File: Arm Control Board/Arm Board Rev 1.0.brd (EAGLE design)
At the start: 189.8 x 119.2 mm, 54 parts

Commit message: test
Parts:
- moved B1 85.2 mm to (78.0, 74.0)
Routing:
- net TX: track 133.4 -> 132.8 mm

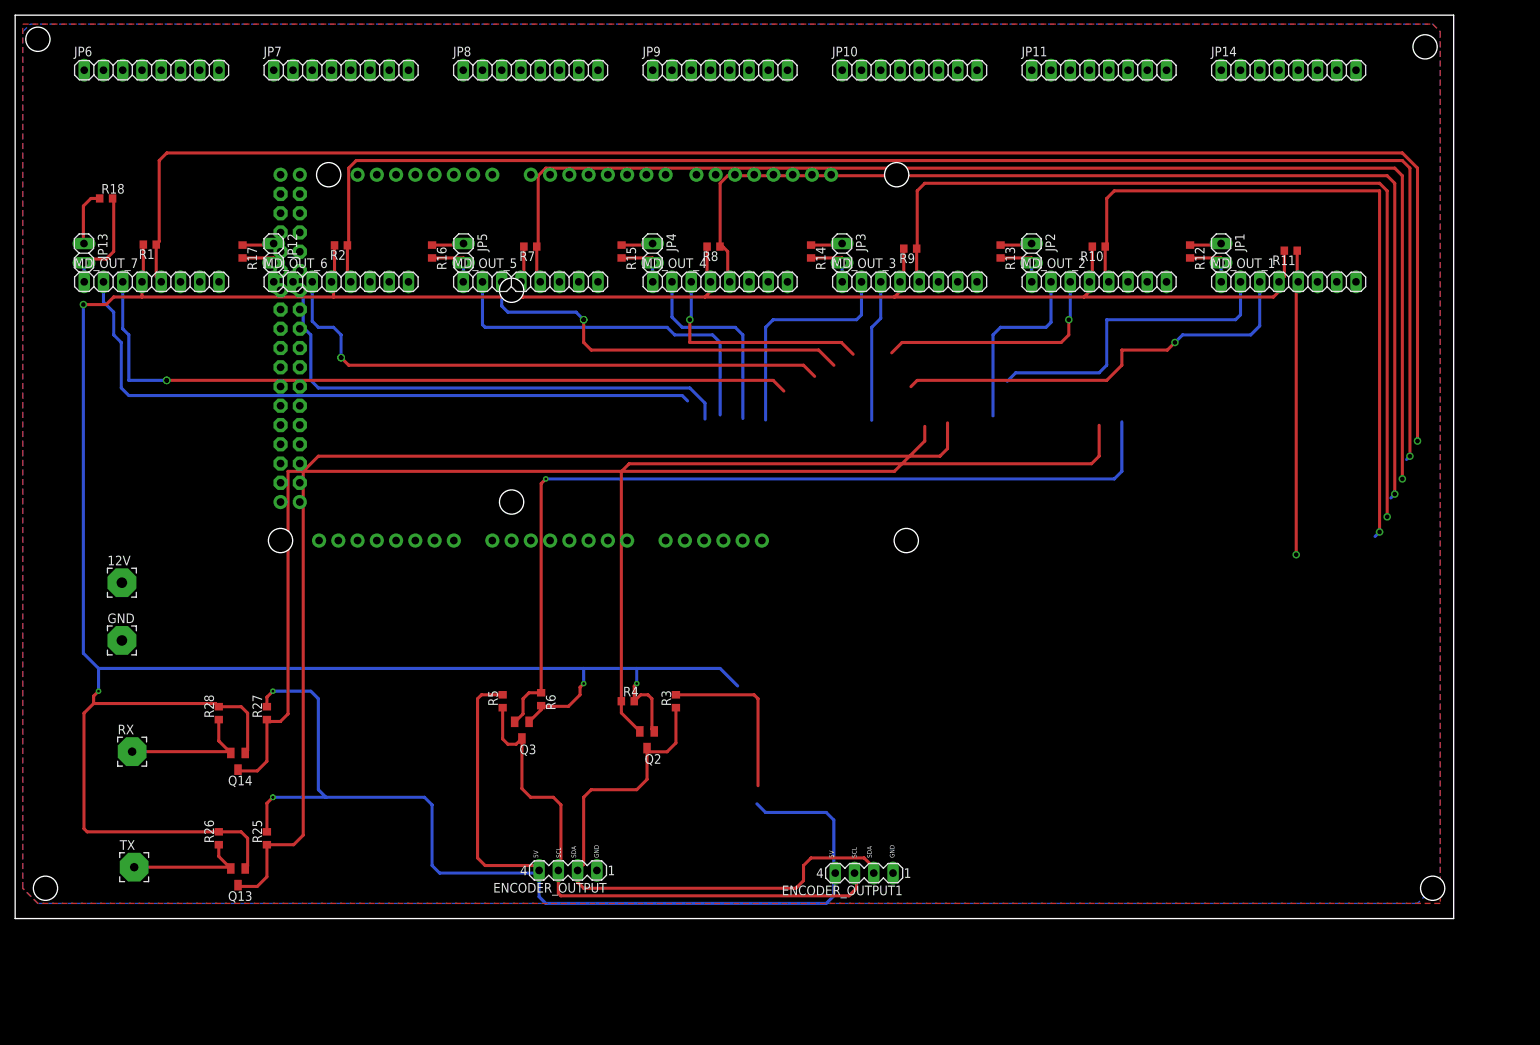
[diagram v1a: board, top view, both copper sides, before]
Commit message: removed tx and rx
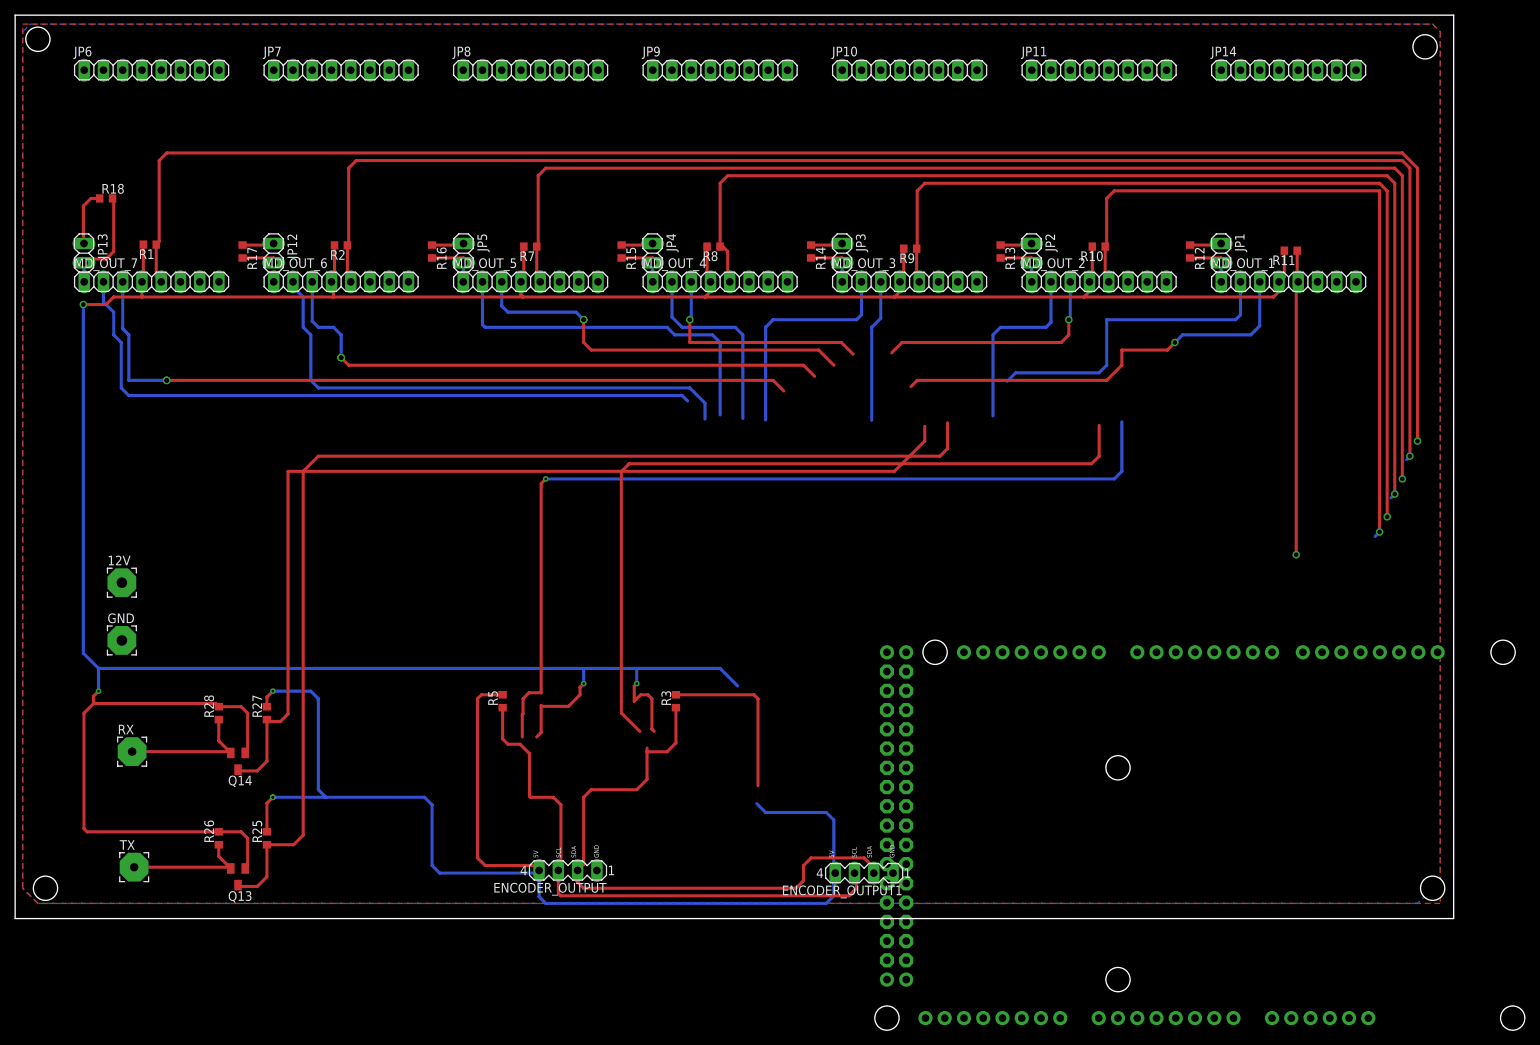
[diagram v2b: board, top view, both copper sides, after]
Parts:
- removed Q2, Q3: (no value), adafruit:SOT23
- removed R4, R6: 10K, rcl:R0603
- R3, R5: value 10K -> 100K
- moved B1 101.8 mm to (158.0, 11.0)
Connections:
- net 3.3V: no longer Q2.1, Q3.1, R4.2, R6.2
- net SCL: no longer Q3.2, R6.1
- net SCL_OUT: no longer Q3.3
- net SDA: no longer Q2.2, R4.1
- net SDA_OUT: no longer Q2.3
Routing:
- net 3.3V: track 439.2 -> 440.8 mm
- net SCL: track 117.7 -> 119.2 mm
- net SCL_OUT: track 73.7 -> 72.5 mm
